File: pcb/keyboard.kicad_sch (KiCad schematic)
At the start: 63 parts, among them J1 Tag-Connect TC2030, J1 USB4510-03-1-A, J4 Battery (JST_S2B-PH-K-S), Q2 2N7002, SW1 PWR, U1 SRV05-4, U3 BQ24075, U3 BT840, Y1 ECS-.327-9-34B-TR

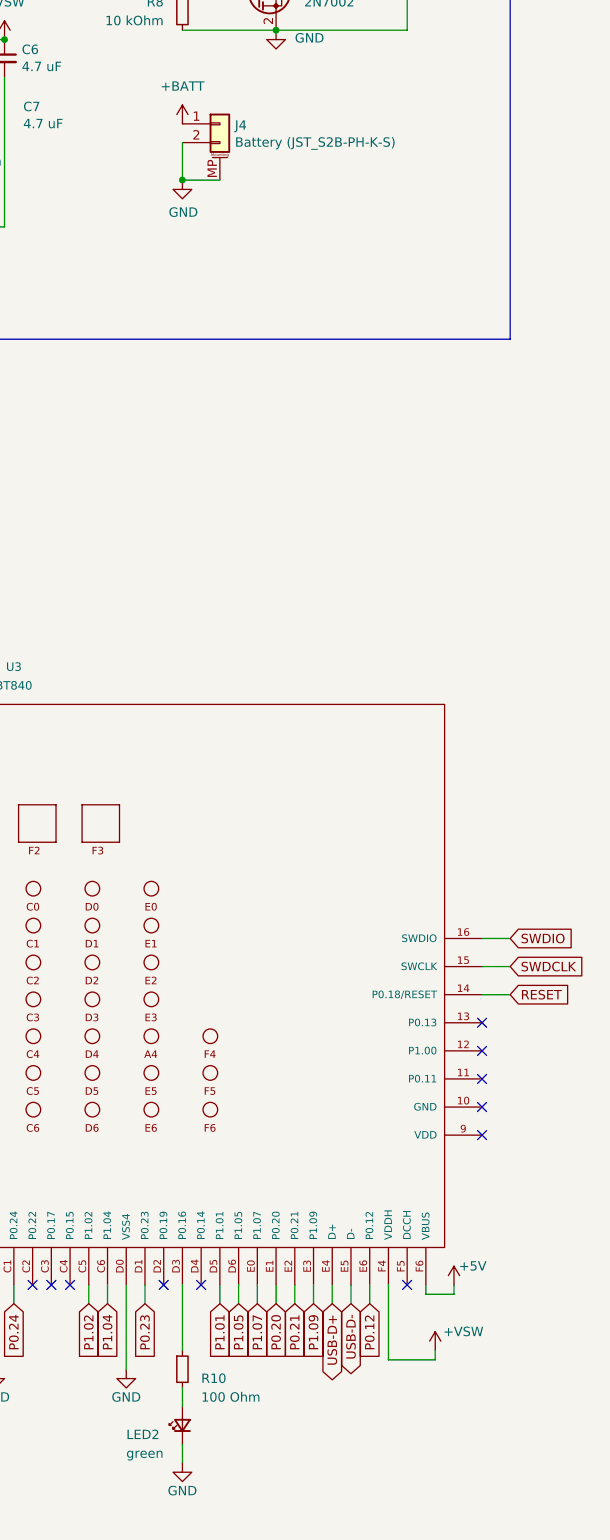
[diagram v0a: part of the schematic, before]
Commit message: #1 Complete BOM information
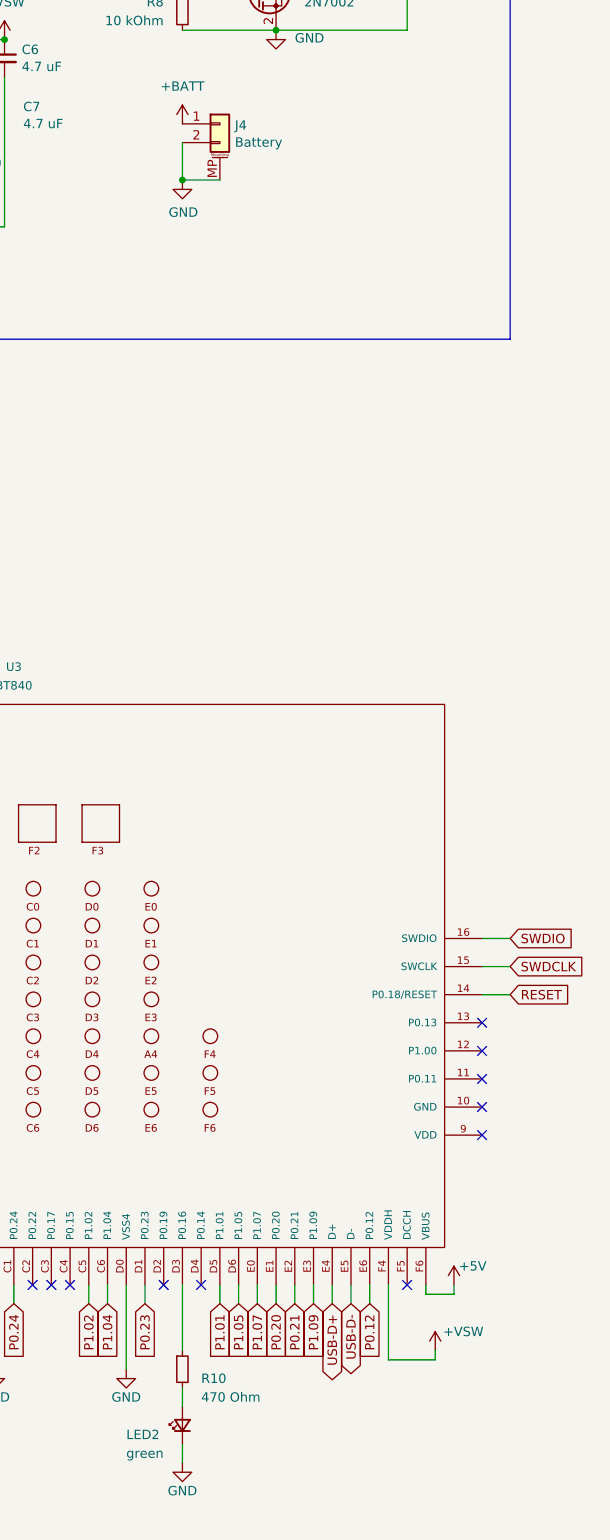
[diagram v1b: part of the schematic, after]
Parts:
- C1: Digikey (none) -> https://www.digikey.fr/short/dfdcwqzh; Mfr Part Number (none) -> CL10B104KB8NNWC; Notes X7R, 10% -> CAP CER 0.1UF 50V X7R 0603
- C5, C6, C7: Digikey (none) -> https://www.digikey.fr/short/9ddcdmj1; Mfr Part Number (none) -> CL10A475KO8NNNC; Notes X7R, 10% -> CAP CER 4.7UF 16V X5R 0603
- C5, C6: Digikey (none) -> https://www.digikey.fr/short/93345tjz; Mfr Part Number (none) -> CC0603JPNPO9BN120; Notes (none) -> CAP CER 12PF 50V C0G/NPO 0603
- D1: Digikey (none) -> https://www.digikey.fr/short/ndftbf2d; Mfr Part Number (none) -> STS321050B100; Notes (none) -> TVS DIODE 5VWM 20VC SOD323
- F1: Digikey (none) -> https://www.digikey.fr/short/8chdpvvc; Mfr Part Number (none) -> ERB-RE0R75V; Notes (none) -> FUSE BOARD MNT 750MA 32VDC 0603
- J1: Digikey (none) -> https://www.digikey.fr/short/t5517rjb; Mfr Part Number (none) -> USB4510-03-1-A; Notes (none) -> USB C REC 16P 3U" MID MNT 1.6MM
- J4: value Battery (JST_S2B-PH-K-S) -> Battery; Mfr Part Number (none) -> JST_S2B-PH-K-S; Notes (none) -> CONN HEADER R/A 2POS 2MM
- L1, L2: Digikey (none) -> https://www.digikey.fr/short/5017v0dz; Mfr Part Number (none) -> BLM18SG121TN1D; Notes (none) -> FERRITE BEAD 120 OHM 0603 1LN
- LED2: Digikey (none) -> https://www.digikey.fr/short/9hh0d35q; Mfr Part Number (none) -> 150060VS55040; Notes (none) -> LED GREEN DIFFUSED 0603 SMD
- LED2: Digikey (none) -> https://www.digikey.fr/short/wn1w0bhr; Mfr Part Number (none) -> LO Q976-PS-25-0-20-R18; Notes (none) -> LED ORANGE DIFFUSED 0603 SMD
- Q2: Digikey (none) -> https://www.digikey.fr/short/2whmm8p2; Mfr Part Number (none) -> 2N7002; Notes (none) -> MOSFET SOT23 N 60V 5OHM 150C
- R1, R2: Digikey (none) -> https://www.digikey.fr/short/n44t24n9; Mfr Part Number (none) -> RC0603FR-135K1L; Notes (none) -> RES 5.1K OHM 1% 1/10W 0603
- R10, R13: Digikey (none) -> https://www.digikey.fr/short/phch2hb9; Mfr Part Number (none) -> RC0603FR-131K5L; Notes (none) -> RES 1.5K OHM 1% 1/10W 0603
- R10: value 100 Ohm -> 470 Ohm; Digikey (none) -> https://www.digikey.fr/short/jp814v51; Mfr Part Number (none) -> RC0603FR-13470RL; Notes (none) -> RES 470 OHM 1% 1/10W 0603
- R11, R8: Digikey (none) -> https://www.digikey.fr/short/q2w0pb82; Mfr Part Number (none) -> RC0603FR-0710KL; Notes (none) -> RES 10K OHM 1% 1/10W 0603
- R12: footprint Resistor_SMD:R_0402_1005Metric -> Resistor_SMD:R_0603_1608Metric; Digikey (none) -> https://www.digikey.fr/short/92pntfd4; Mfr Part Number (none) -> RC0603FR-1347KL; Notes (none) -> RES 47K OHM 1% 1/10W 0603
- R14: Digikey (none) -> https://www.digikey.fr/short/d7m30hjz; Mfr Part Number (none) -> RC0603FR-105K6L; Notes (none) -> RES 5.6K OHM 1% 1/10W 0603
- R3: Digikey (none) -> https://www.digikey.fr/short/z45v3mjc; Mfr Part Number (none) -> RC0603FR-071ML; Notes (none) -> RES 1M OHM 1% 1/10W 0603
- R4: Digikey (none) -> https://www.digikey.fr/short/3j5f0vnv; Mfr Part Number (none) -> RC0603FR-07100KL; Notes (none) -> RES 100K OHM 1% 1/10W 0603
- R5: Digikey (none) -> https://www.digikey.fr/short/b2zjwm5d; Mfr Part Number (none) -> RC0603FR-07100RL; Notes (none) -> RES 100 OHM 1% 1/10W 0603
- S1, S10, S11, S12, S13, S14, S15, S16, S17, S18, S19, S2, S20, S21, S22, S23, S24, S25, S26, S27, S28, S29, S3, S4, S5, S6, S7, S8, S9: Digikey (none) -> https://splitkb.com/collections/switches-and-keycaps/produc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; Mfr Part Number (none) -> KLH-CHC-BRN-010; Notes (none) -> Kailh Low Profile Choc Switches (Brown (50gf, Tactile))
- S30: Notes (none) -> SWITCH TACTILE SPST-NO 0.05A 24V
- SW1: Notes (none) -> SWITCH SLIDE SPDT 300MA 6V
- U1: Digikey (none) -> https://www.digikey.fr/short/p7hw7bpv; Mfr Part Number (none) -> SRV05-4; Notes (none) -> TVS DIODE 5V VBR MIN 6V SOT-23
- U3: Digikey (none) -> https://www.digikey.fr/short/cn0mz24p; Mfr Part Number (none) -> BQ24075RGTR; Notes (none) -> IC BATT CHG LI-ION 1CELL 16QFN
- U3: Digikey (none) -> https://www.digikey.fr/short/4qd39n5h; Mfr Part Number (none) -> BT840; Notes (none) -> RF TXRX MODULE BT TRACE ANT SMD
- Y1: Mfr Part Number (none) -> ECS-.327-9-34B-TR

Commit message: #1 Reorganize the schematic
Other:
- note added: "MCU - nRF52840"
- moved on the sheet: C5, C6, C7, J1, J4, LED2, Q2, R10, R11, R12, R13, R14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

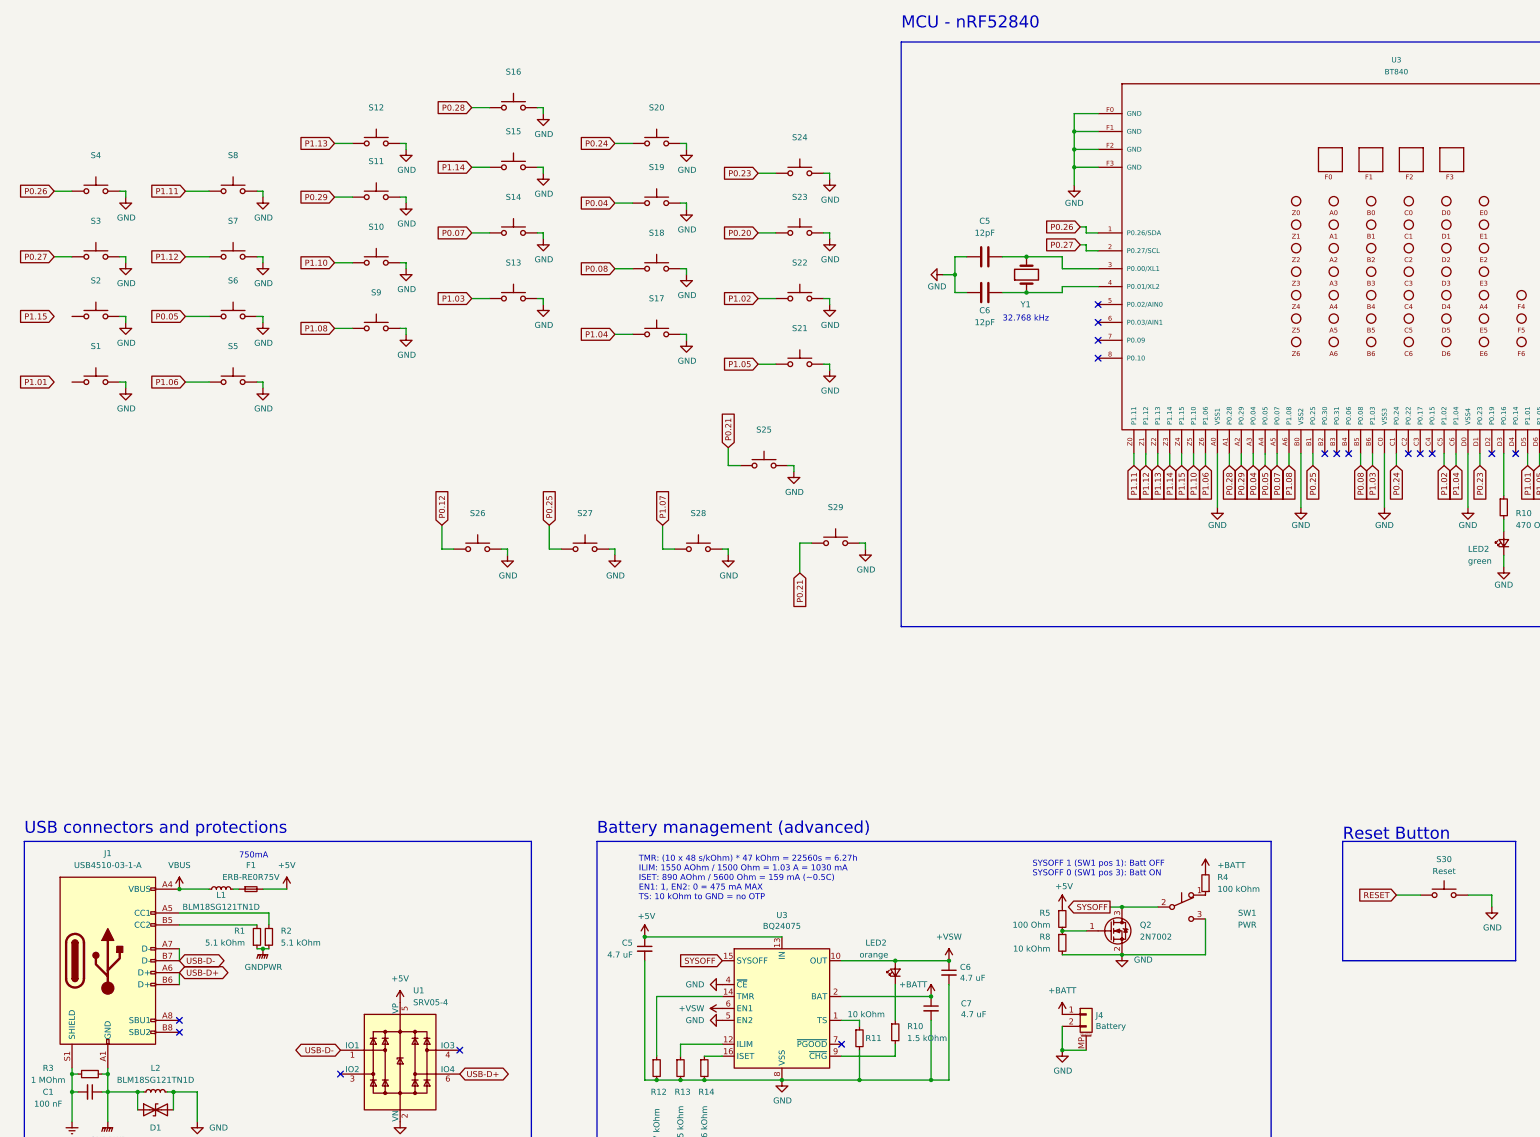
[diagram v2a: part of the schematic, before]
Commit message: #1 Reassign component references
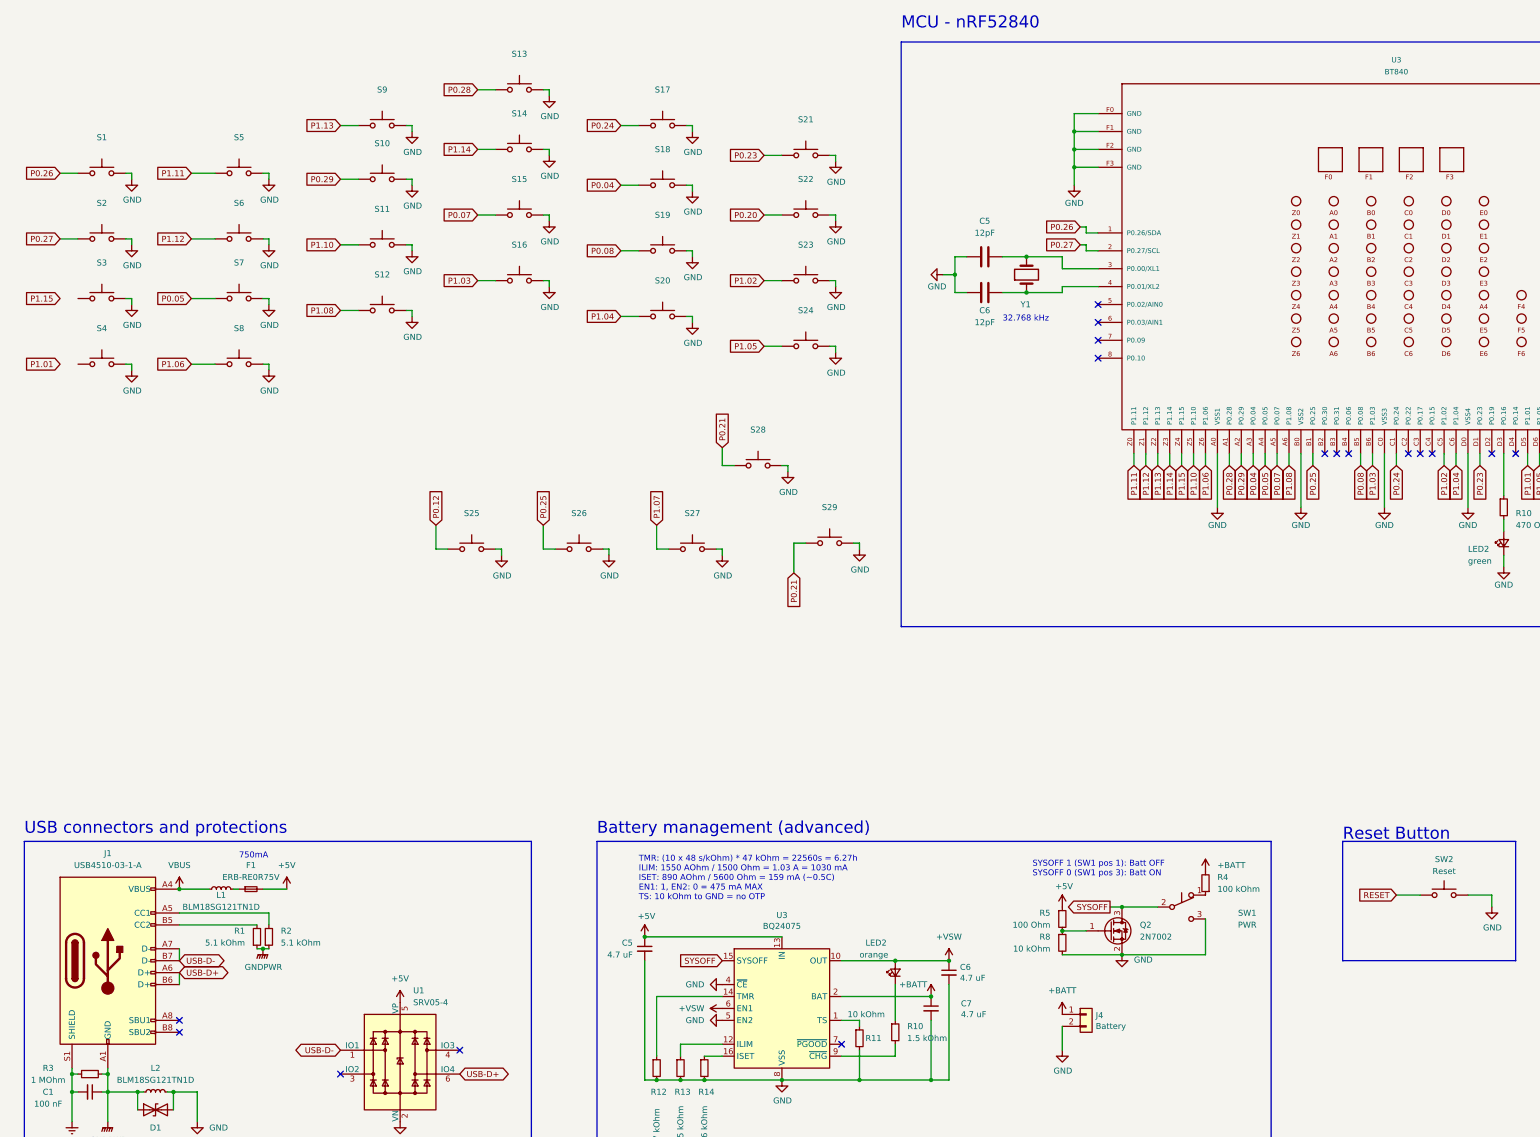
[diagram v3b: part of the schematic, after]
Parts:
- J4: symbol Connector_Generic_MountingPin:Conn_01x02_MountingPin -> Connector_Generic:Conn_01x02
- renumbered S4 to S1, S11 to S10, S10 to S11, S9 to S12, S16 to S13, S15 to S14, S14 to S15, S13 to S16, S20 to S17, S19 to S18, S18 to S19, S3 to S2, S17 to S20, S24 to S21, S23 to S22, S22 to S23, S21 to S24, S26 to S25, S27 to S26, S28 to S27, S25 to S28, S2 to S3, S1 to S4, S8 to S5, S7 to S6, S6 to S7, S5 to S8, S12 to S9, S30 to SW2
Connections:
- net GND: no longer J4.MP (MountPin)
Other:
- moved on the sheet: S1, S10, S11, S12, S13, S14, S15, S16, S17, S18, S19, S2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

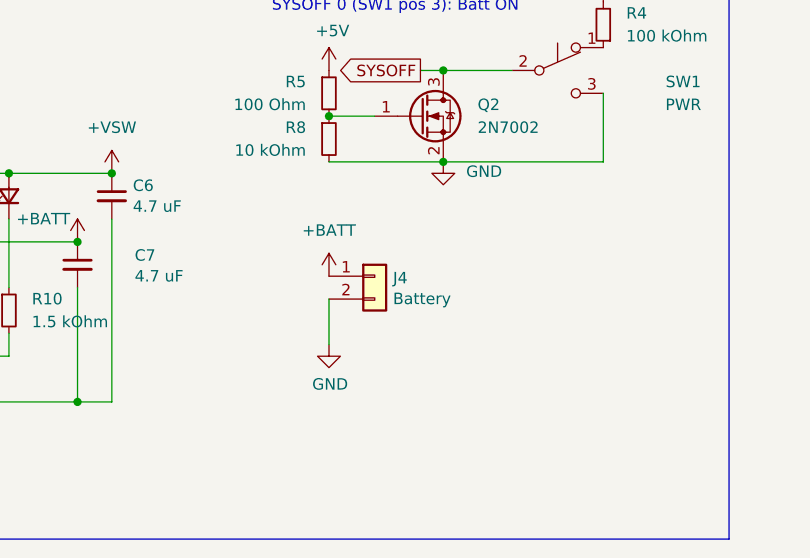
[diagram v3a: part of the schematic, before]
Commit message: #2 Expand the PCB to accomodate all components
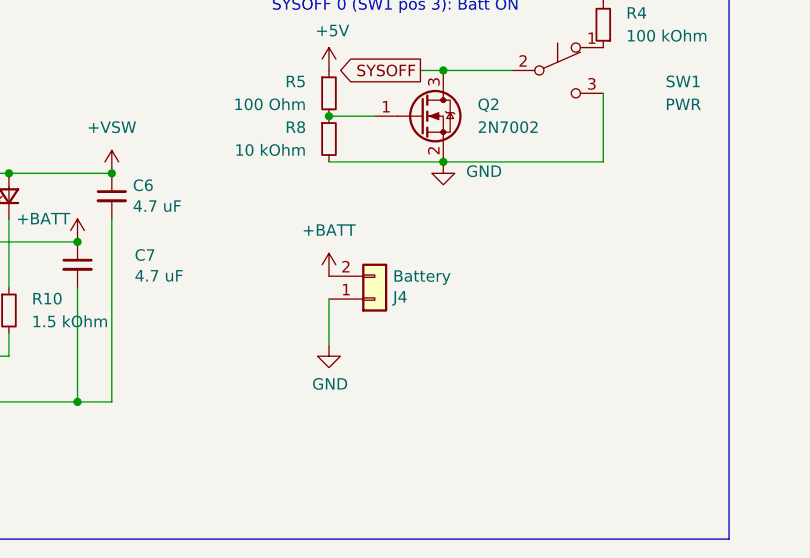
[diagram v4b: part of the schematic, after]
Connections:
- net +BATT: now also J4.2 (Pin_2); no longer J4.1 (Pin_1)
- net GND: now also J4.1 (Pin_1); no longer J4.2 (Pin_2)
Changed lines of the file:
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@@
     )
   )
-  (symbol (lib_id "Connector_Generic:Conn_01x02") (at 247.65 246.38 0) (unit 1)
+  (symbol (lib_id "Connector_Generic:Conn_01x02") (at 247.65 248.92 0) (mirror x) (unit 1)
     (in_bom yes) (on_board yes) (dnp no)
-    (property "Reference" "J4" (at 249.682 246.5832 0)
+    (property "Reference" "J4" (at 249.682 248.7168 0)
       (effects (font (size 1.27 1.27)) (justify left))
     )
-    (property "Value" "Battery" (at 249.682 248.8946 0)
+    (property "Value" "Battery" (at 249.682 246.4054 0)
       (effects (font (size 1.27 1.27)) (justify left))
     )
-    (property "Footprint" "Connector_JST:JST_PH_S2B-PH-K_1x02_P2.00mm_Horizontal" (at 247.65 246.38 0)
+    (property "Footprint" "Connector_JST:JST_PH_S2B-PH-K_1x02_P2.00mm_Horizontal" (at 247.65 248.92 0)
       (effects (font (size 1.27 1.27)) hide)
     )
-    (property "Datasheet" "~" (at 247.65 246.38 0)
+    (property "Datasheet" "~" (at 247.65 248.92 0)
       (effects (font (size 1.27 1.27)) hide)
     )
-    (property "Digikey" "https://www.digikey.fr/short/4nfzf328" (at 247.65 246.38 0)
+    (property "Digikey" "https://www.digikey.fr/short/4nfzf328" (at 247.65 248.92 0)
       (effects (font (size 1.27 1.27)) hide)
     )
-    (property "Mfr Part Number" "JST_S2B-PH-K-S" (at 247.65 246.38 0)
+    (property "Mfr Part Number" "JST_S2B-PH-K-S" (at 247.65 248.92 0)
       (effects (font (size 1.27 1.27)) hide)
     )
-    (property "Notes" "CONN HEADER R/A 2POS 2MM" (at 247.65 246.38 0)
+    (property "Notes" "CONN HEADER R/A 2POS 2MM" (at 247.65 248.92 0)
       (effects (font (size 1.27 1.27)) hide)
     )
